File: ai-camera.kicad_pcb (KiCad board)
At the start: 4 copper layers, 70 x 70 mm, 166 parts, among them J1 Conn-01x02_P2mm_S2B-PH-K-S_Ho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, J2 USB_B_Micro_10118194-0001LF, J3 DBG, J4 Conn-02x10_P2.54mm_B-2100S20P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, J5 Conn-01x02_P1.25mm_10114829-1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, J6 Conn_01x24_FFC_0.5mm_hirose_F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, J7 Conn_01x24_FFC_0.5mm_hirose_F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, Q1 AO3401A, Q2 AO3400A, Q3 AO3400A, Q4 AO3401A, Q5 AO3400A, Q6 AO3401A, Q7 AO3400A, Q8 AO3400A, SW1 SW_PB_TS-1187A-B-A-B, SW2 SW_PB_TS-1187A-B-A-B, SW3 SW_PB_TS-1187A-B-A-B, SW4 SW_PB_TS-1187A-B-A-B, U1 SRV05-4, U10 AP1511B, U11 ESP32-S3-WROOM-1-N16R8, U12 MT9284-28J, U2 TP4057-42-SOT26-R, U3 PCF8563T/5,518, U4 XC6206-2.8V, U5 PIR_BS612, U6 SY8089AAAC, U7 SOT-23-6_SN74LVC1G373DBVR_TI, U8 XC6206-2.8V, U9 RT9166-12GVL, Y1 32.768kHz_Q13FC1350000400

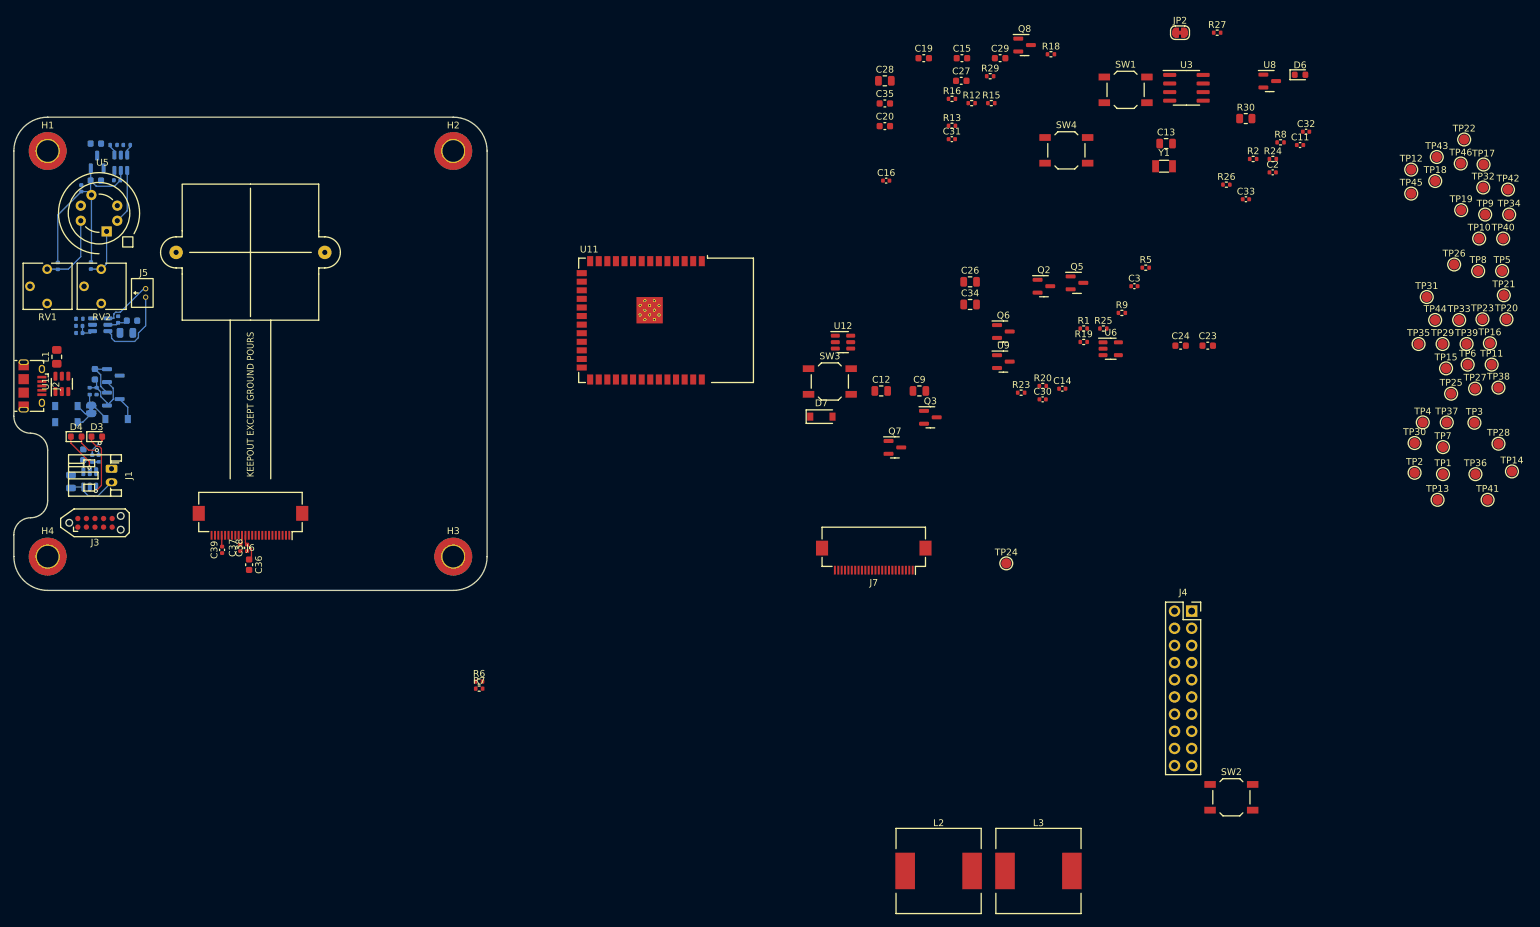
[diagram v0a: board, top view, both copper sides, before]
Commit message: ai camera layout: prelim DC-DC, change inductors, IR placement
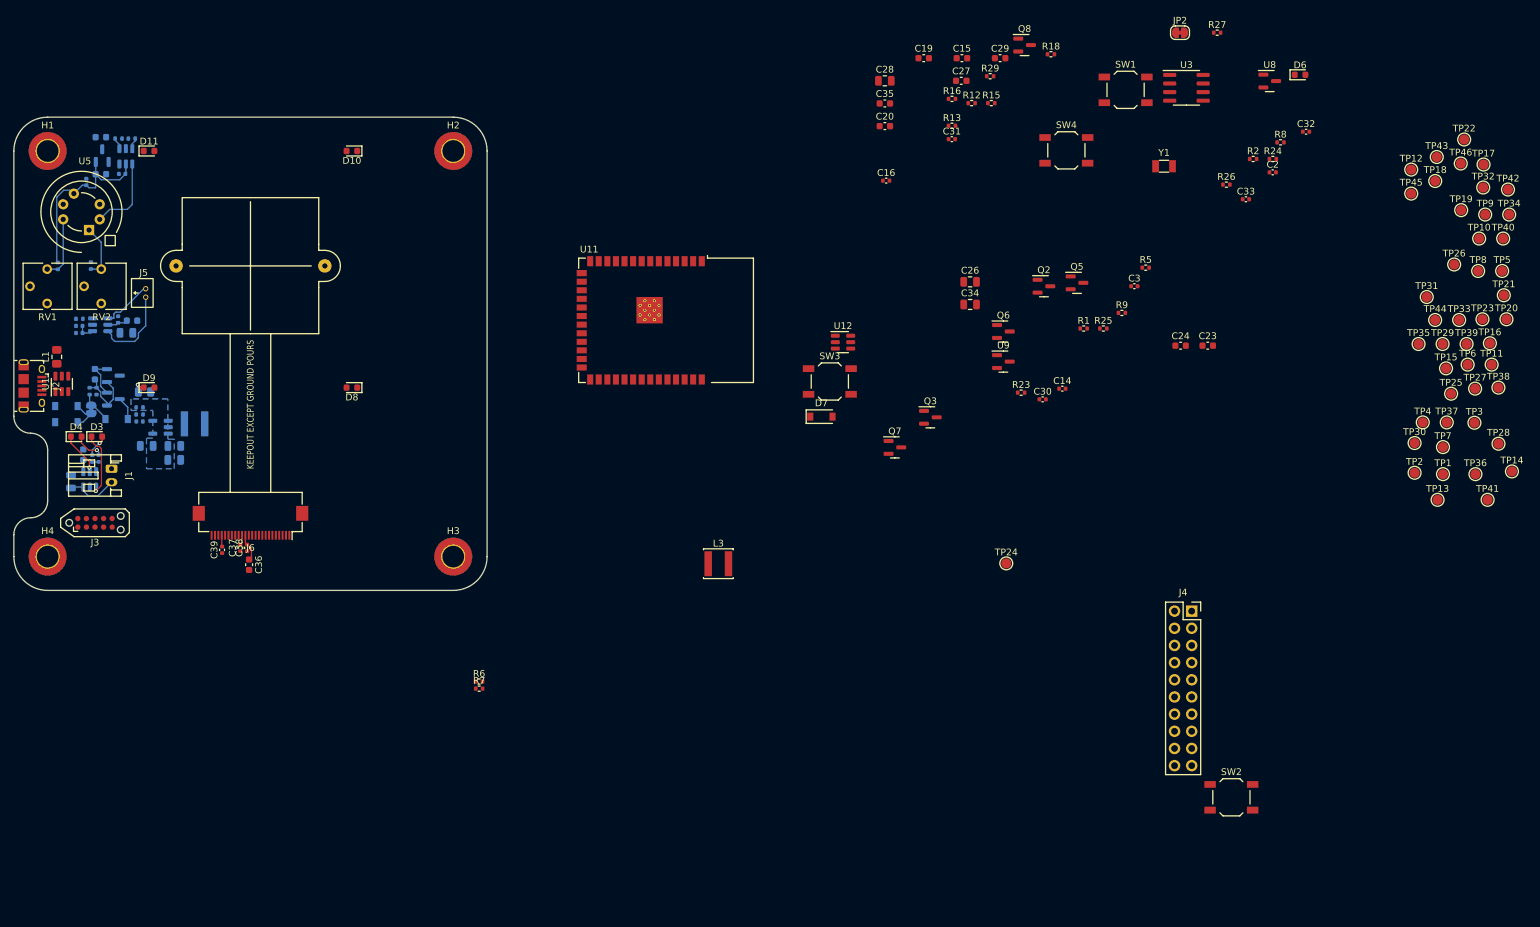
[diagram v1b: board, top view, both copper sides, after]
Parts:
- removed J7: Conn_01x24_FFC_0.5mm_hirose_FH12-24S-0.5SH, 00-kiml-connector-fpc-ffc:Hirose_FH12-24S-0.5SH_1x24-1MP_P0.50mm_Horizontal
- added D10: 0603_IR_850nm_E6C0603IRAC1UDA, LED_SMD:LED_0603_1608Metric, F.Cu at (145.0, 50.0)
- added D11: 0603_IR_850nm_E6C0603IRAC1UDA, LED_SMD:LED_0603_1608Metric, F.Cu at (115.0, 50.0)
- added D8: 0603_IR_850nm_E6C0603IRAC1UDA, LED_SMD:LED_0603_1608Metric, F.Cu at (145.0, 85.0)
- added D9: 0603_IR_850nm_E6C0603IRAC1UDA, LED_SMD:LED_0603_1608Metric, F.Cu at (115.0, 85.0)
- C11, C12, C13, C9, R19, R20, R30, U6: moved to B.Cu
- L2: value 15u_SWRB1205S-150MT -> 10u_SWPA4030S100MT; footprint 00-kiml-inductor-smd:L_12x12mm_H6mm -> Inductor_SMD:L_Sunlord_SWPA40xxS; moved to B.Cu
- L3: value 15u_SWRB1205S-150MT -> 10u_SWPA4030S100MT; footprint 00-kiml-inductor-smd:L_12x12mm_H6mm -> Inductor_SMD:L_Sunlord_SWPA40xxS
- moved C11 176.5 mm to (113.6, 90.0)
- moved R30 167.9 mm to (114.3, 85.7), turned to 180 degrees
- moved C13 154.0 mm to (118.7, 95.7), turned to 180 degrees
- moved U6 141.0 mm to (116.7, 90.9), turned to 180 degrees
- moved R19 140.1 mm to (113.6, 89.0)
- moved R20 133.6 mm to (113.6, 87.9), turned to 180 degrees
- moved L2 128.4 mm to (121.7, 90.4)
- moved C9 114.6 mm to (114.7, 93.6)
- moved C12 104.9 mm to (118.7, 93.6), turned to 180 degrees
- moved L3 65.6 mm to (199.2, 111.0)
- moved U5 2.61 mm to (105.0, 59.0)
- moved REF** 2.00 mm to (130.0, 67.0)
- moved C5 1.20 mm to (107.9, 48.0)
- moved C7 1.20 mm to (107.9, 53.4)
- moved C8 1.20 mm to (105.7, 54.6)
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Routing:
- net /PWR_PIR: track 34.2 -> 27.5 mm
- net Net-(U5-Pad2): track 8.05 -> 11.7 mm
- net Net-(R30-Pad2): track 0.00 -> 2.17 mm, vias 0 -> 1
- net Net-(R14-Pad2): track 11.1 -> 9.32 mm
- net Net-(R17-Pad2): track 7.44 -> 8.06 mm
- added copper zone on B.Cu, net GND

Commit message: ai camera layout: more LEDs, better caps to address LED driver voltage output
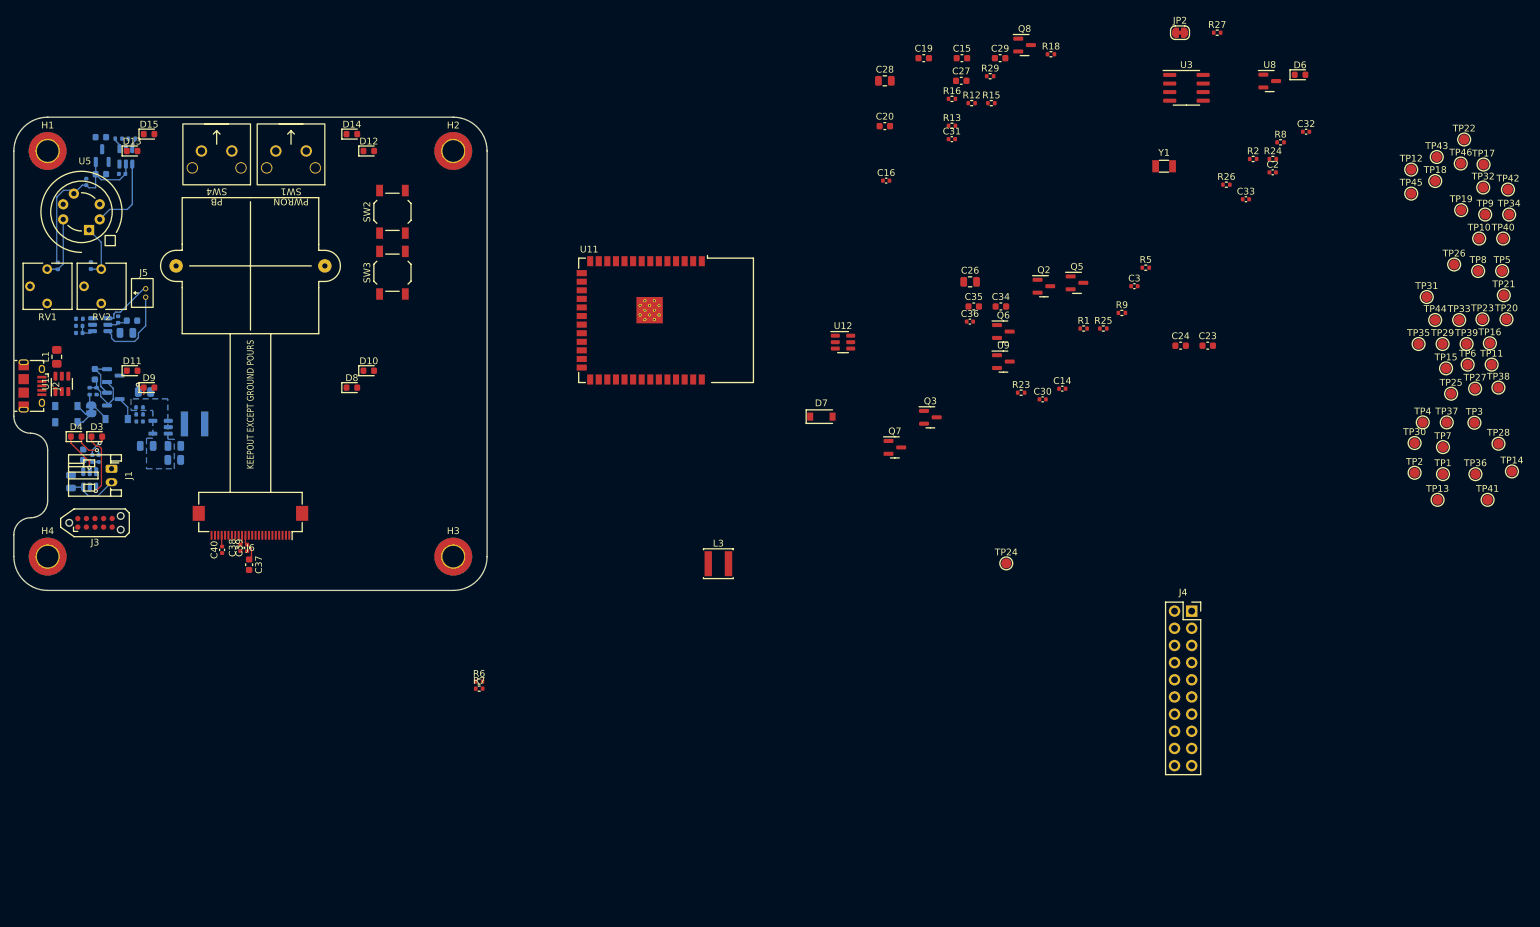
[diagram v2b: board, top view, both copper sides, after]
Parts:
- added C36: 100n_0402_CL05B104KB54PNC, Capacitor_SMD:C_0402_1005Metric, F.Cu at (236.4, 75.2)
- added D12: 0603_IR_850nm_E6C0603IRAC1UDA, LED_SMD:LED_0603_1608Metric, F.Cu at (147.5, 50.0)
- added D13: 0603_IR_850nm_E6C0603IRAC1UDA, LED_SMD:LED_0603_1608Metric, F.Cu at (112.5, 50.0)
- added D14: 0603_IR_850nm_E6C0603IRAC1UDA, LED_SMD:LED_0603_1608Metric, F.Cu at (145.0, 47.5)
- added D15: 0603_IR_850nm_E6C0603IRAC1UDA, LED_SMD:LED_0603_1608Metric, F.Cu at (115.0, 47.5)
- C1, C15, C19, C20, C22, C23, C24, C27, C29, C35, C5, C6, C7: value 10u_0603_CL10A106KP8NNNC -> 10u_0603_CL10A106MA8NRNC
- C34: value 22u_0805_CL21A226MAQNNNE -> 10u_0603_CL10A106MA8NRNC; footprint Capacitor_SMD:C_0805_2012Metric -> Capacitor_SMD:C_0603_1608Metric
- C37: renamed from C36; value 10u_0603_CL10A106KP8NNNC -> 10u_0603_CL10A106MA8NRNC
- SW1, SW4: value SW_PB_TS-1187A-B-A-B -> SW_PB_90deg_K2-1102AQ-H4CW-01; footprint Button_Switch_SMD:SW_SPST_TL3342 -> 00-kiml-button-switch-tht:SW_PB_90deg_K2-1102AQ-H4CW-01
- moved SW2 151.3 mm to (151.0, 59.0), turned to 90 degrees
- moved SW4 125.7 mm to (125.0, 50.0), turned to 180 degrees
- moved SW1 123.8 mm to (136.0, 50.0), turned to 180 degrees
- moved SW3 66.7 mm to (151.0, 68.0), turned to 90 degrees
- moved C35 32.8 mm to (237.0, 73.0)
- moved D10 32.6 mm to (147.5, 82.5), turned to 0 degrees
- moved D11 32.6 mm to (112.5, 82.5)
- moved C34 4.56 mm to (241.0, 73.0)
- turned D8 to 0 degrees
- renumbered C37 to C38, C38 to C39, C39 to C40
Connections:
- C35 pad 1: GND -> Net-(D7-Pad1)
- D11 pad 2: Net-(D10-Pad1) -> Net-(D11-Pad2)
- D7 pad 1: Net-(C34-Pad2) -> Net-(D7-Pad1)
- D8 pad 2: Net-(C34-Pad2) -> Net-(D7-Pad1)
- U12 pad 5: Net-(C34-Pad2) -> Net-(D7-Pad1)
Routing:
- net Net-(R30-Pad2): track 2.17 -> 3.17 mm

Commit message: ai camera layout: ALS selected and prelim component placement
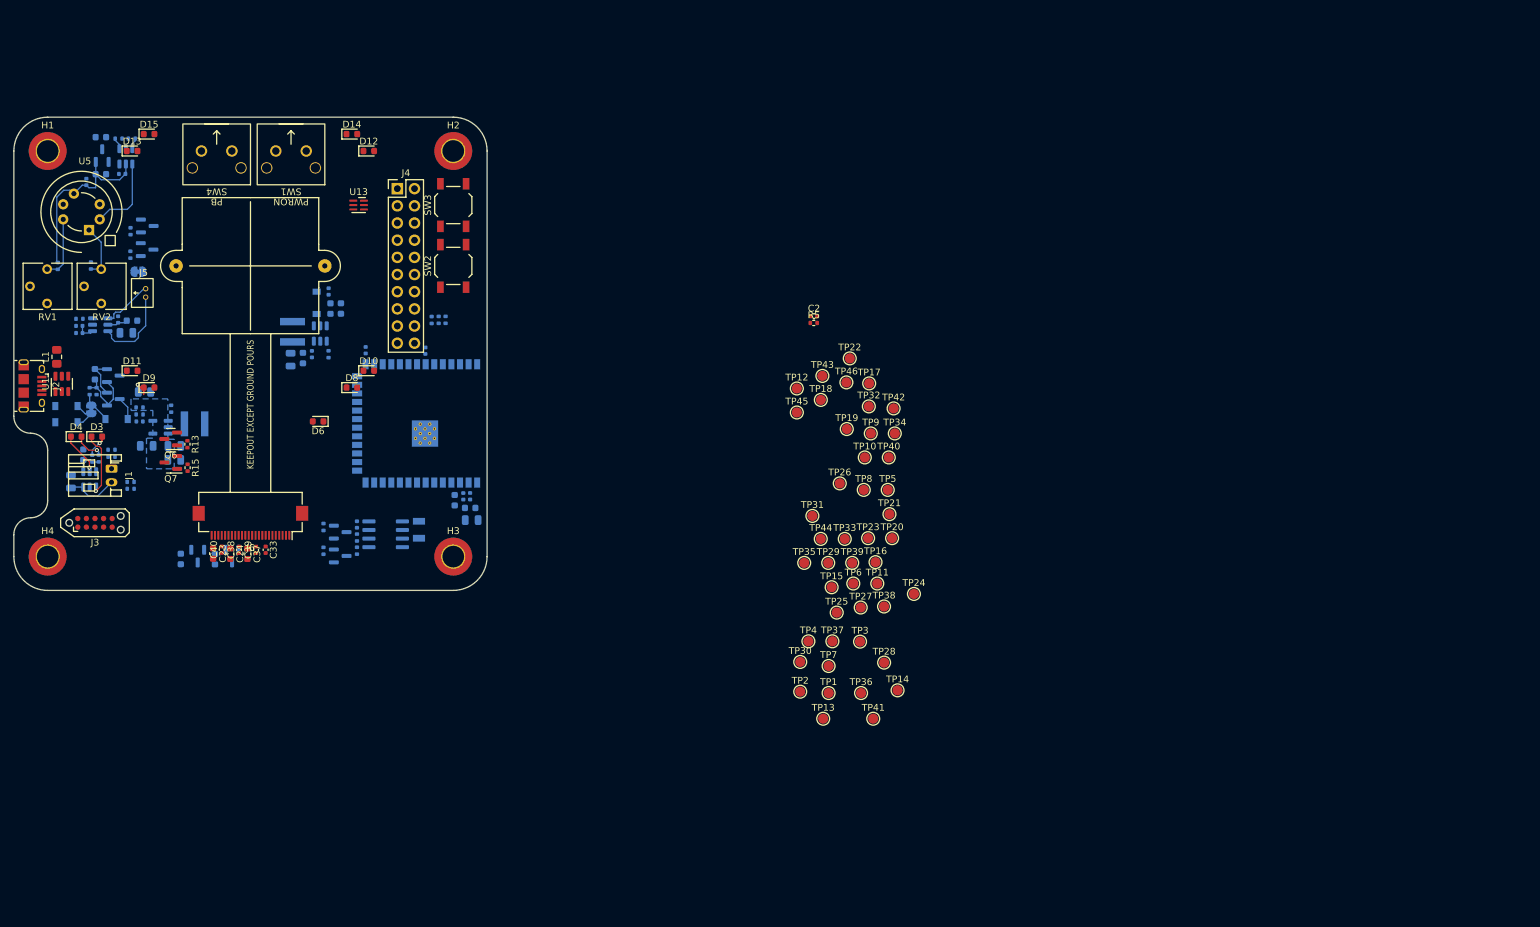
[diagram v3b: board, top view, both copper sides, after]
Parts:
- added U13: APDS-9306-065, 00-kiml-optical:Broadcom_DFN-6_2x2mm_P0.65mm, F.Cu at (146.0, 58.0)
- C14, C15, C16, C19, C20, C26, C27, C28, C29, C3, C30, C31, C32, C34, C35, C36, D7, JP2, L3, Q2, Q3, Q5, Q8, R1, R12, R16, R18, R2, R23, R24, R25, R26, R27, R29, R6, R7, R8, R9, U11, U12, U3, U8, U9, Y1: moved to B.Cu
- J4: footprint Connector_PinSocket_2.54mm:PinSocket_2x10_P2.54mm_Vertical -> Connector_PinHeader_2.54mm:PinHeader_2x10_P2.54mm_Vertical
- moved U8 173.4 mm to (122.2, 109.9), turned to -90 degrees
- moved R2 173.1 mm to (112.3, 100.0), turned to 180 degrees
- moved JP2 158.1 mm to (113.4, 67.8), turned to 180 degrees
- moved D6 154.0 mm to (140.0, 90.0), turned to 180 degrees
- moved C33 154.0 mm to (132.2, 109.0), turned to -90 degrees
- moved R24 151.9 mm to (140.8, 109.1), turned to -90 degrees
- moved C23 150.3 mm to (124.5, 109.5), turned to -90 degrees
- moved R8 148.6 mm to (145.8, 107.2), turned to -90 degrees
- moved C24 143.9 mm to (127.0, 109.6), turned to -90 degrees
- moved R1 142.8 mm to (112.3, 99.0)
- moved R18 138.6 mm to (112.3, 61.9), turned to -90 degrees
- moved Q5 137.6 mm to (114.7, 64.6)
- moved U3 135.6 mm to (150.0, 106.7), turned to 180 degrees
- moved C32 134.9 mm to (162.5, 101.1), turned to -90 degrees
- moved J4 133.1 mm to (151.7, 55.6)
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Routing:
- net +3V3: track 7.13 -> 3.04 mm
- net +2V8: track 1.69 -> 0.00 mm
- net +1V2: track 1.47 -> 0.00 mm

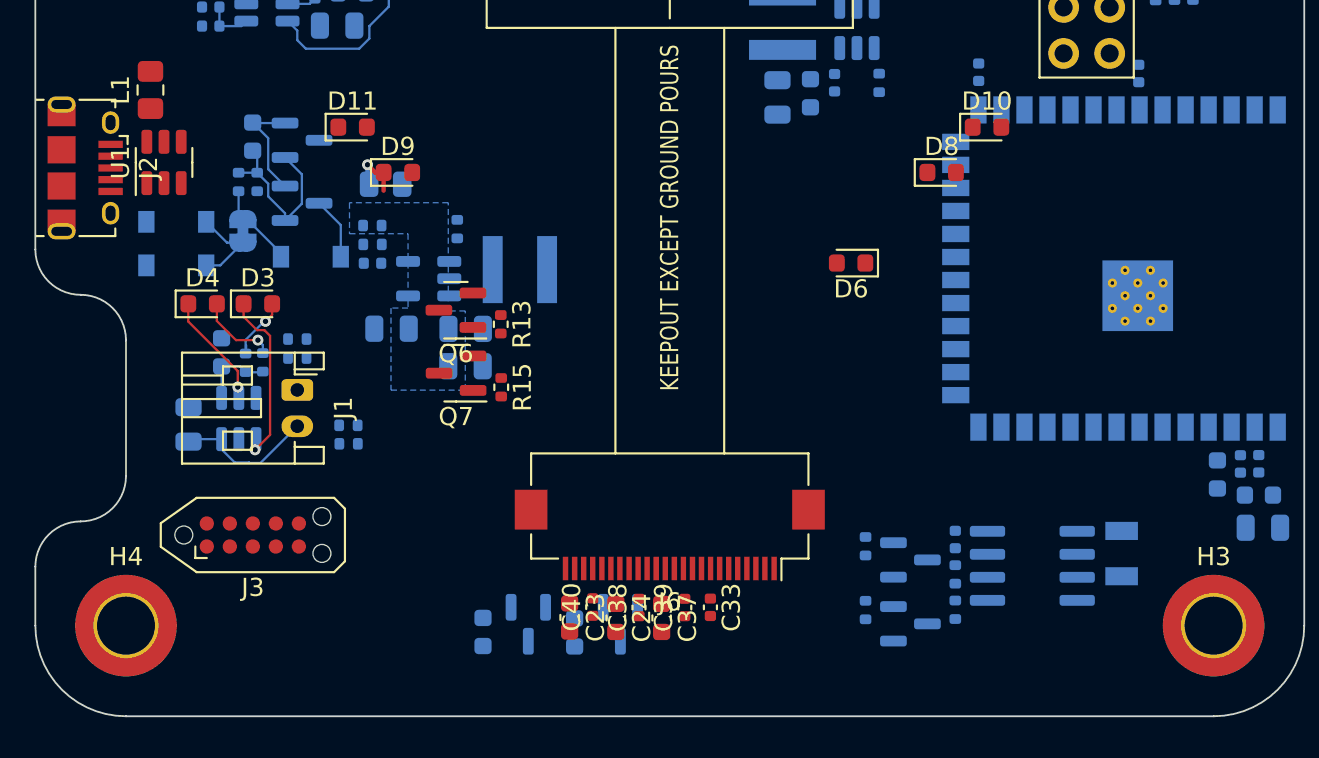
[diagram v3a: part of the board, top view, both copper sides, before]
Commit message: ai camera layout: route high speed camera and diffpair
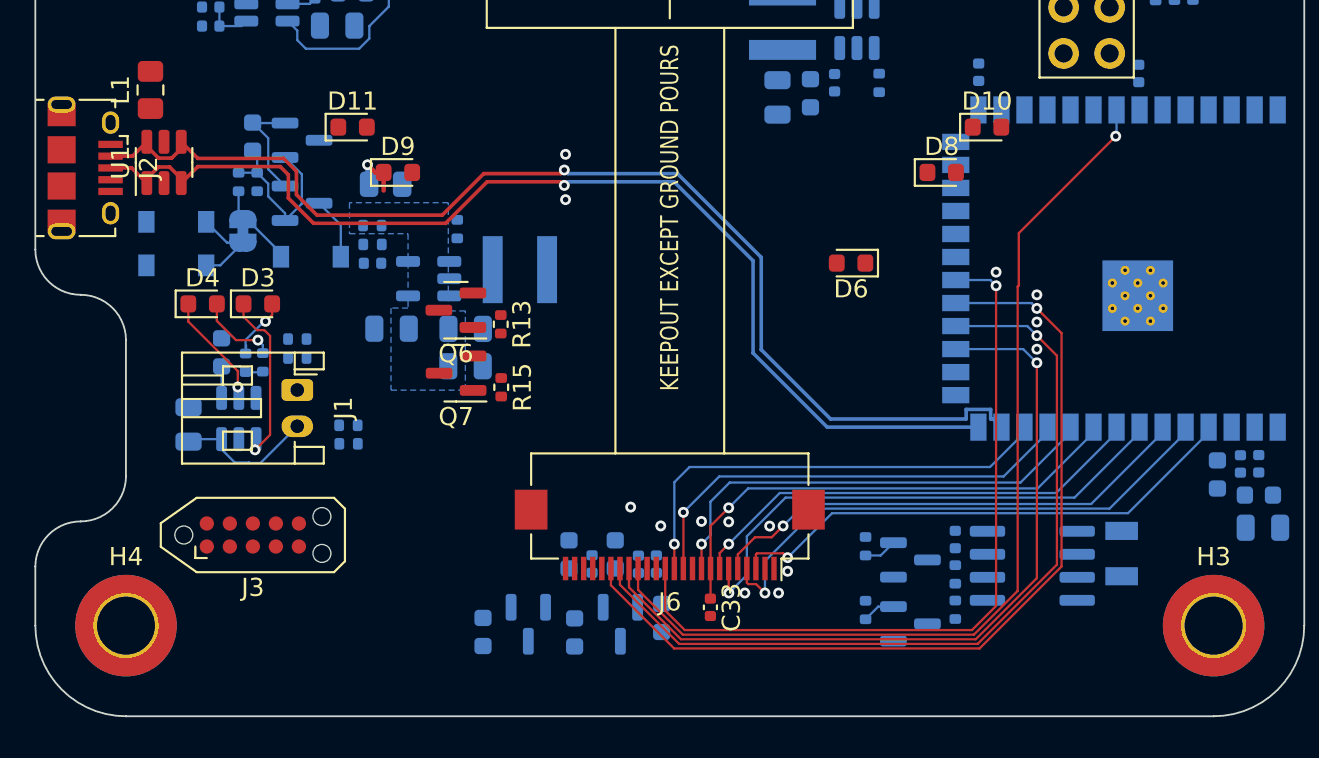
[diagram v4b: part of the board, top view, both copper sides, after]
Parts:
- C23, C24, C37, C38, C39, C40: moved to B.Cu
- moved C24 3.51 mm to (127.0, 106.1), turned to 90 degrees
- moved C23 3.48 mm to (124.4, 106.1), turned to 90 degrees
- moved C39 2.86 mm to (129.3, 106.6), turned to -90 degrees
- moved C38 2.38 mm to (128.3, 106.6), turned to -90 degrees
- moved C40 2.38 mm to (125.7, 106.6), turned to -90 degrees
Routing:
- net /UD-: track 0.00 -> 63.9 mm, vias 0 -> 1
- net /UD+: track 0.00 -> 61.4 mm, vias 0 -> 1
- net /CAM.HREF: track 0.00 -> 52.9 mm, vias 0 -> 1
- net /CAM.RST: track 0.00 -> 48.5 mm, vias 0 -> 1
- net /CAM.VSYNC: track 0.00 -> 45.9 mm, vias 0 -> 1
- net /CAM.PWDN: track 0.00 -> 42.8 mm, vias 0 -> 1
- net /CAM.D9: track 0.00 -> 41.6 mm, vias 0 -> 1
- net /CAM.D3: track 0.00 -> 30.2 mm, vias 0 -> 1
- net /CAM.D2: track 0.00 -> 29.2 mm, vias 0 -> 1
- net /CAM.D4: track 0.00 -> 29.0 mm, vias 0 -> 1
- net /CAM.PCLK: track 0.00 -> 27.6 mm, vias 0 -> 1
- net /CAM.D5: track 0.00 -> 27.3 mm, vias 0 -> 1
- net /CAM.D6: track 0.00 -> 25.8 mm, vias 0 -> 1
- net /CAM.D7: track 0.00 -> 25.6 mm, vias 0 -> 1
- net /CAM.MCLK: track 0.00 -> 25.5 mm, vias 0 -> 1
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- added copper zone on In1.Cu, net GND
- added copper zone on In2.Cu, net GND
